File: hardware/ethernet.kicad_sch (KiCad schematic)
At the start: 41 parts, among them J1 J0011D21BNL, U22 W5500, U7 USBLC6-2P6, U9 USBLC6-2P6, Y65 25MHz

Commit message: Debugging LED added
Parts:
- R1, R12, R13, R15, R16, R17, R18, R19, R20, R21, R22, R23, R8, R80: footprint Resistor_SMD:R_0603_1608Metric -> Resistor_SMD:R_0805_2012Metric
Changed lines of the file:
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@@
 			)
 		)
-		(property "Footprint" "Resistor_SMD:R_0603_1608Metric"
+		(property "Footprint" "Resistor_SMD:R_0805_2012Metric"
 			(at 157.48 110.49 0)
 			(effects
@@
 			)
 		)
-		(property "Footprint" "Resistor_SMD:R_0603_1608Metric"
+		(property "Footprint" "Resistor_SMD:R_0805_2012Metric"
 			(at 143.51 135.89 0)
 			(effects
@@
 			)
 		)
-		(property "Footprint" "Resistor_SMD:R_0603_1608Metric"
+		(property "Footprint" "Resistor_SMD:R_0805_2012Metric"
 			(at 200.66 142.24 0)
 			(effects
@@
 			)
 		)
-		(property "Footprint" "Resistor_SMD:R_0603_1608Metric"
+		(property "Footprint" "Resistor_SMD:R_0805_2012Metric"
 			(at 128.27 92.71 0)
 			(effects
@@
 			)
 		)
-		(property "Footprint" "Resistor_SMD:R_0603_1608Metric"
+		(property "Footprint" "Resistor_SMD:R_0805_2012Metric"
 			(at 177.8 72.39 0)
 			(effects
@@
 			)
 		)
-		(property "Footprint" "Resistor_SMD:R_0603_1608Metric"
+		(property "Footprint" "Resistor_SMD:R_0805_2012Metric"
 			(at 68.58 110.49 0)
 			(effects
@@
 			)
 		)
-		(property "Footprint" "Resistor_SMD:R_0603_1608Metric"
+		(property "Footprint" "Resistor_SMD:R_0805_2012Metric"
 			(at 128.27 99.06 0)
 			(effects
@@
 			)
 		)
-		(property "Footprint" "Resistor_SMD:R_0603_1608Metric"
+		(property "Footprint" "Resistor_SMD:R_0805_2012Metric"
 			(at 160.02 72.39 0)
 			(effects
@@
 			)
 		)
-		(property "Footprint" "Resistor_SMD:R_0603_1608Metric"
+		(property "Footprint" "Resistor_SMD:R_0805_2012Metric"
 			(at 148.59 110.49 0)
 			(effects
@@
 			)
 		)
-		(property "Footprint" "Resistor_SMD:R_0603_1608Metric"
+		(property "Footprint" "Resistor_SMD:R_0805_2012Metric"
 			(at 58.42 118.11 0)
 			(effects
@@
 			)
 		)
-		(property "Footprint" "Resistor_SMD:R_0603_1608Metric"
+		(property "Footprint" "Resistor_SMD:R_0805_2012Metric"
 			(at 168.91 72.39 0)
 			(effects
@@
 			)
 		)
-		(property "Footprint" "Resistor_SMD:R_0603_1608Metric"
+		(property "Footprint" "Resistor_SMD:R_0805_2012Metric"
 			(at 128.27 80.01 0)
 			(effects
@@
 			)
 		)
-		(property "Footprint" "Resistor_SMD:R_0603_1608Metric"
+		(property "Footprint" "Resistor_SMD:R_0805_2012Metric"
 			(at 201.93 134.62 0)
 			(effects
@@
 			)
 		)
-		(property "Footprint" "Resistor_SMD:R_0603_1608Metric"
+		(property "Footprint" "Resistor_SMD:R_0805_2012Metric"
 			(at 128.27 86.36 0)
 			(effects

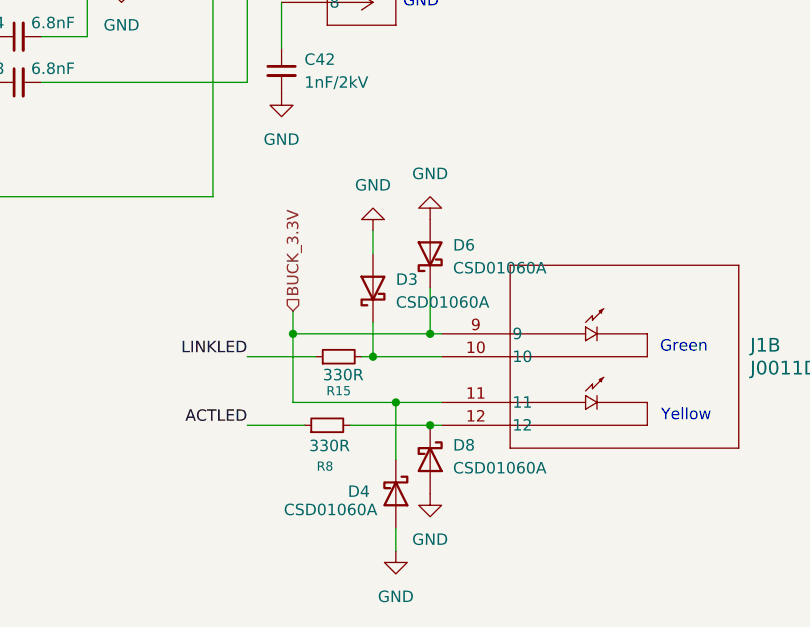
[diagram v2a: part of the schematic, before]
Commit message: removed Ethernet LED diodes
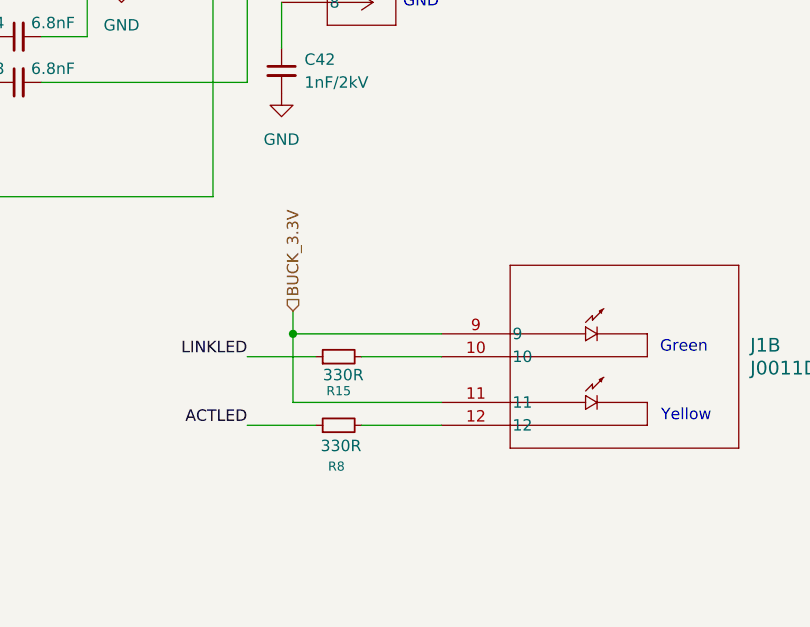
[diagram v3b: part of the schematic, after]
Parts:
- removed D3, D4, D6, D8: CSD01060A, Package_TO_SOT_THT:TO-220-2_Vertical, symbol Diode:CSD01060A
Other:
- moved on the sheet: R8

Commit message: Replaced 3.3V symbol
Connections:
- net BUCK_3.3V renamed +3.3V

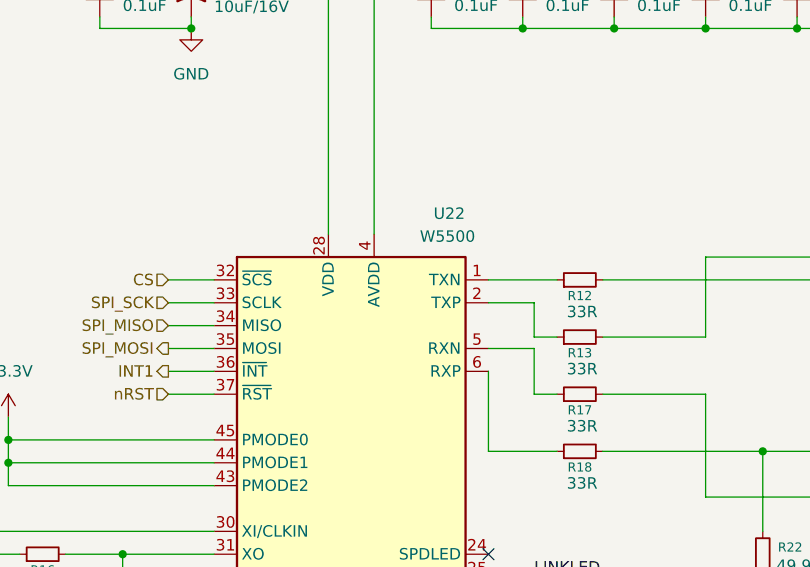
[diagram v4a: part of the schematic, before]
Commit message: updated major symbol and footprints
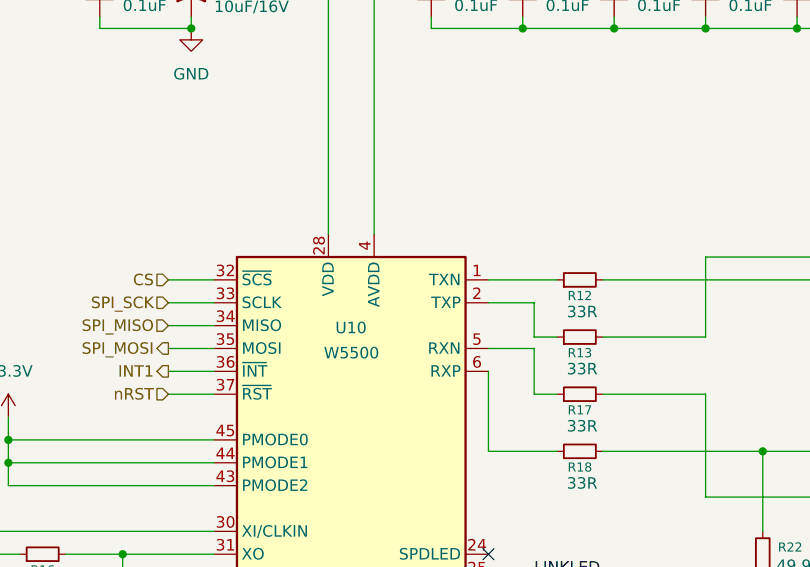
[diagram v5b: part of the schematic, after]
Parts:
- removed U22: W5500, Package_QFP:LQFP-48_7x7mm_P0.5mm, symbol Interface_Ethernet:W5500
- added U10: W5500, Package_QFP:LQFP-48_7x7mm_P0.5mm, symbol Interface_Ethernet:W5500
- J1: footprint Custom_Parts:CONN_J0011D21B_PUL -> pyronet_footprints:CONN_J0011D21B_PUL; symbol 2026-02-18_03-44-30:J0011D21BNL -> pyronet_symbols:J0011D21BNL
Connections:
- net +3.3V: now also U10.28 (VDD), U10.43 (PMODE2), U10.44 (PMODE1), U10.45 (PMODE0)
- net +3.3VA: now also U10.11 (AVDD), U10.15 (AVDD), U10.17 (AVDD), U10.21 (AVDD), U10.4 (AVDD), U10.8 (AVDD)
- net ACTLED: now also U10.27 (ACTLED)
- net CS: now also U10.32 (~{SCS})
- net GND: now also U10.14 (AGND), U10.16 (AGND), U10.19 (AGND), U10.29 (GND), U10.3 (AGND), U10.48 (AGND), U10.9 (AGND)
- net INT1: now also U10.36 (~{INT})
- net LINKLED: now also U10.25 (LINKLED)
- net SPI_MISO: now also U10.34 (MISO)
- net SPI_MOSI: now also U10.35 (MOSI)
- net SPI_SCK: now also U10.33 (SCLK)
- net nRST: now also U10.37 (~{RST})
- net at C29.1: now also U10.20 (TOCAP)
- net at R1.1: now also U10.10 (EXRES1)
- net at C28.1: now also U10.22 (1V2O)
- net at R17.1: now also U10.5 (RXN)
- net at R12.1: now also U10.1 (TXN)
- net at R13.1: now also U10.2 (TXP)
- net at R16.1, R80.1: now also U10.30 (XI/CLKIN)
- net at C8.1, R16.2, Y65.3: now also U10.31 (XO)
- net at R18.1: now also U10.6 (RXP)
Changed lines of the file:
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@@
 	)
 	(symbol
-		(lib_id "2026-02-18_03-44-30:J0011D21BNL")
+		(lib_id "pyronet_symbols:J0011D21BNL")
 		(at 213.36 132.08 0)
 		(unit 2)
@@
 			)
 		)
-		(property "Footprint" "Custom_Parts:CONN_J0011D21B_PUL"
+		(property "Footprint" "pyronet_footprints:CONN_J0011D21B_PUL"
 			(at 213.36 132.08 0)
 			(effects
@@
 	)
 	(symbol
-		(lib_id "Interface_Ethernet:W5500")
-		(at 102.87 105.41 0)
-		(unit 1)
-		(exclude_from_sim no)
-		(in_bom yes)
-		(on_board yes)
-		(dnp no)
-		(property "Reference" "U22"
-			(at 112.014 72.644 0)
-			(effects
-				(font
-					(size 1.27 1.27)
-				)
-				(justify left)
-			)
-		)
-		(property "Value" "W5500"
-			(at 110.49 75.184 0)
-			(effects
-				(font
-					(size 1.27 1.27)
-				)
-				(justify left)
-			)
-		)
-		(property "Footprint" "Package_QFP:LQFP-48_7x7mm_P0.5mm"
-			(at 102.87 63.5 0)
-			(effects
-				(font
-					(size 1.27 1.27)
-				)
-				(hide yes)
-			)
-		)
-		(property "Datasheet" "http://wizwiki.net/wiki/lib/exe/fetch.php/products:w5500:w5500_ds_v109e.pdf"
-			(at 102.87 80.01 0)
-			(effects
-				(font
-					(size 1.27 1.27)
-				)
-				(hide yes)
-			)
-		)
-		(property "Description" "10/100Mb SPI Ethernet controller with TCP/IP stack, LQFP-48"
-			(at 102.87 105.41 0)
-			(effects
-				(font
-					(size 1.27 1.27)
-				)
-				(hide yes)
-			)
-		)
-		(pin "36"
-		)
-		(pin "45"
-		)
-		(pin "30"
-		)
-		(pin "38"
-		)
-		(pin "40"
-		)
-		(pin "42"
-		)
-		(pin "34"
-		)
-		(pin "32"
-		)
-		(pin "35"
-		)
-		(pin "33"
-		)
-		(pin "37"
-		)
-		(pin "44"
-		)
-		(pin "43"
-		)
-		(pin "31"
-		)
-		(pin "39"
-		)
-		(pin "41"
-		)
-		(pin "19"
-		)
-		(pin "3"
-		)
-		(pin "1"
-		)
-		(pin "26"
-		)
-		(pin "28"
-		)
-		(pin "46"
-		)
-		(pin "20"
-		)
-		(pin "11"
-		)
-		(pin "17"
-		)
-		(pin "14"
-		)
-		(pin "16"
-		)
-		(pin "13"
-		)
-		(pin "2"
-		)
-		(pin "23"
-		)
-		(pin "29"
-		)
-		(pin "15"
-		)
-		(pin "4"
-		)
-		(pin "8"
-		)
-		(pin "12"
-		)
-		(pin "9"
-		)
-		(pin "7"
-		)
-		(pin "47"
-		)
-		(pin "21"
-		)
-		(pin "5"
-		)
-		(pin "48"
-		)
-		(pin "6"
-		)
-		(pin "24"
-		)
-		(pin "25"
-		)
-		(pin "27"
-		)
-		(pin "10"
-		)
-		(pin "18"
-		)
-		(pin "22"
-		)
-		(instances
-			(project "Senior_Design"
-				(path "/8f5928e8-0fc1-4443-a20f-3bfeb956761e/d4b85e6c-5f5c-4400-806e-353edbeb9b74"
-					(reference "U22")
-					(unit 1)
-				)
-			)
-		)
-	)
-	(symbol
 		(lib_id "Device:C_Small")
 		(at 166.37 99.06 90)
@@
 	)
 	(symbol
+		(lib_id "Interface_Ethernet:W5500")
+		(at 102.87 105.41 0)
+		(unit 1)
+		(exclude_from_sim no)
+		(in_bom yes)
+		(on_board yes)
+		(dnp no)
+		(property "Reference" "U10"
+			(at 101.092 85.344 0)
+			(effects
+				(font
+					(size 1.27 1.27)
+				)
+				(justify left)
+			)
+		)
+		(property "Value" "W5500"
+			(at 99.822 88.138 0)
+			(effects
+				(font
+					(size 1.27 1.27)
+				)
+				(justify left)
+			)
+		)
+		(property "Footprint" "Package_QFP:LQFP-48_7x7mm_P0.5mm"
+			(at 102.87 63.5 0)
+			(effects
+				(font
+					(size 1.27 1.27)
+				)
+				(hide yes)
+			)
+		)
+		(property "Datasheet" "http://wizwiki.net/wiki/lib/exe/fetch.php/products:w5500:w5500_ds_v109e.pdf"
+			(at 102.87 80.01 0)
+			(effects
+				(font
+					(size 1.27 1.27)
+				)
+				(hide yes)
+			)
+		)
+		(property "Description" "10/100Mb SPI Ethernet controller with TCP/IP stack, LQFP-48"
+			(at 102.87 105.41 0)
+			(effects
+				(font
+					(size 1.27 1.27)
+				)
+				(hide yes)
+			)
+		)
+		(pin "32"
+		)
+		(pin "21"
+		)
+		(pin "14"
+		)
+		(pin "19"
+		)
+		(pin "4"
+		)
+		(pin "16"
+		)
+		(pin "8"
+		)
+		(pin "3"
+		)
+		(pin "48"
+		)
+		(pin "17"
+		)
+		(pin "43"
+		)
+		(pin "35"
+		)
+		(pin "44"
+		)
+		(pin "45"
+		)
+		(pin "37"
+		)
+		(pin "36"
+		)
+		(pin "34"
+		)
+		(pin "30"
+		)
+		(pin "15"
+		)
+		(pin "11"
+		)
+		(pin "29"
+		)
+		(pin "28"
+		)
+		(pin "23"
+		)
+		(pin "42"
+		)
+		(pin "41"
+		)
+		(pin "40"
+		)
+		(pin "39"
+		)
+		(pin "38"
+		)
+		(pin "31"
+		)
+		(pin "33"
+		)
+		(pin "9"
+		)
+		(pin "7"
+		)
+		(pin "12"
+		)
+		(pin "13"
+		)
+		(pin "46"
+		)
+		(pin "47"
+		)
+		(pin "1"
+		)
+		(pin "2"
+		)
+		(pin "5"
+		)
+		(pin "6"
+		)
+		(pin "24"
+		)
+		(pin "25"
+		)
+		(pin "26"
+		)
+		(pin "27"
+		)
+		(pin "10"
+		)
+		(pin "18"
+		)
+		(pin "20"
+		)
+		(pin "22"
+		)
+		(instances
+			(project ""
+				(path "/8f5928e8-0fc1-4443-a20f-3bfeb956761e/d4b85e6c-5f5c-4400-806e-353edbeb9b74"
+					(reference "U10")
+					(unit 1)
+				)
+			)
+		)
+	)
+	(symbol
 		(lib_id "Device:R_Small")
 		(at 68.58 110.49 90)
@@
 	)
 	(symbol
-		(lib_name "J0011D21BNL_1")
-		(lib_id "2026-02-18_03-44-30:J0011D21BNL")
+		(lib_id "pyronet_symbols:J0011D21BNL")
 		(at 195.58 77.47 0)
 		(unit 1)
@@
 			)
 		)
-		(property "Footprint" "Custom_Parts:CONN_J0011D21B_PUL"
+		(property "Footprint" "pyronet_footprints:CONN_J0011D21B_PUL"
 			(at 195.58 77.47 0)
 			(effects

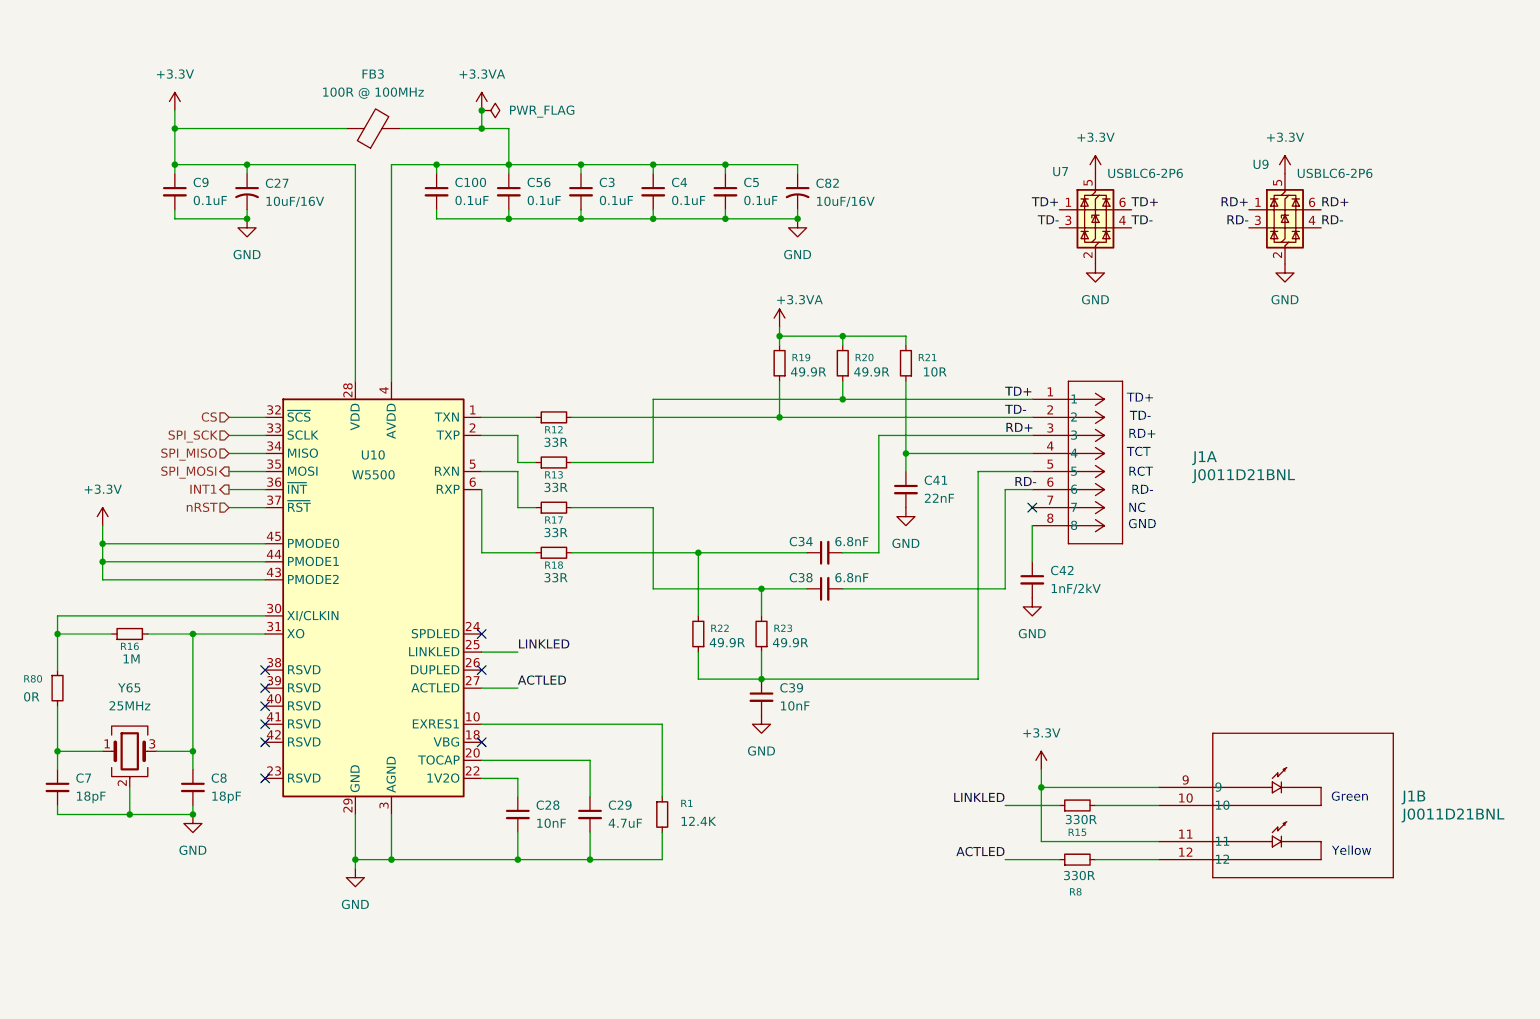
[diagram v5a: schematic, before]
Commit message: updated 5V power and pin
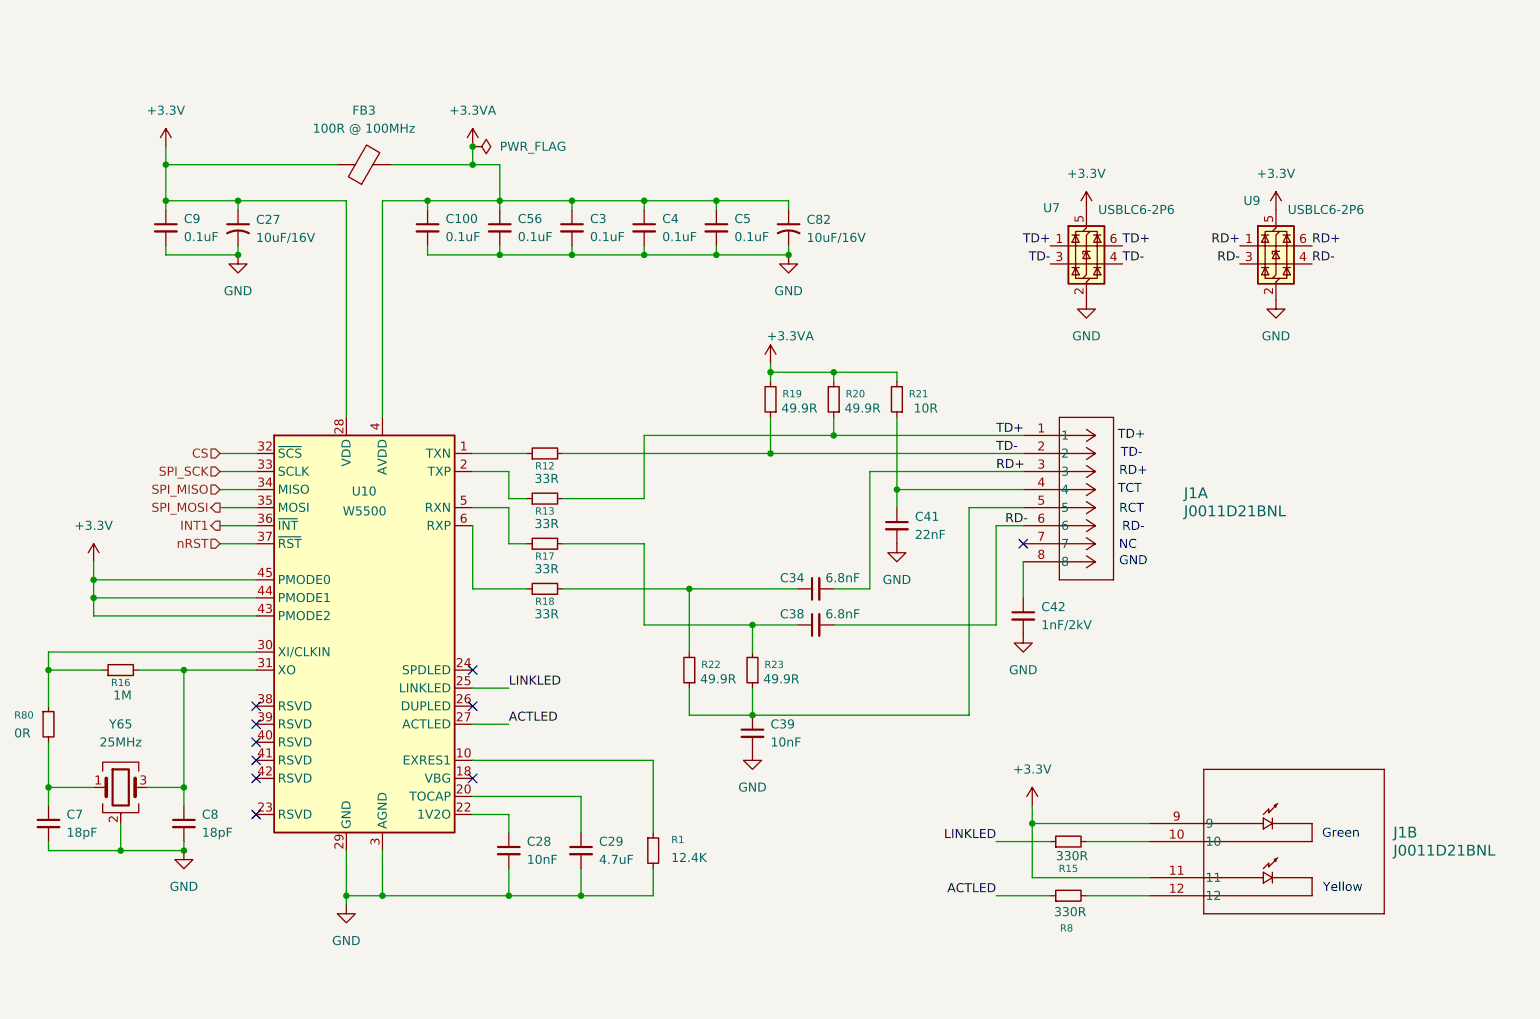
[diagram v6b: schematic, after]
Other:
- moved on the sheet: C100, C27, C28, C29, C3, C34, C38, C39, C4, C41, C42, C5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

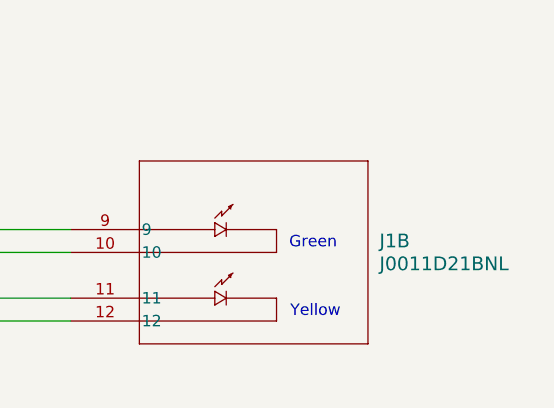
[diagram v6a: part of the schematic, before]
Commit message: passing ERC w/ exclusions
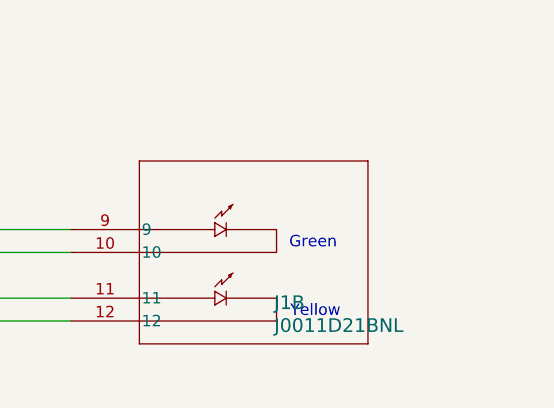
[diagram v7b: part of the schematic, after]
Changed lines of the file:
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@@
 		(fields_autoplaced yes)
 		(property "Reference" "J1"
-			(at 246.38 138.4299 0)
+			(at 234.696 145.288 0)
 			(effects
 				(font
@@
 		)
 		(property "Value" "J0011D21BNL"
-			(at 246.38 140.9699 0)
+			(at 234.696 147.828 0)
 			(effects
 				(font
@@
 	)
 	(symbol
+		(lib_name "J0011D21BNL_1")
 		(lib_id "pyronet_symbols:J0011D21BNL")
 		(at 194.31 82.55 0)

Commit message: updated annotations
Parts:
- renumbered C7 to C701, C9 to C702, C8 to C703, C27 to C704, C100 to C705, C56 to C706, C28 to C707, C3 to C708, C29 to C709, C4 to C710, C5 to C711, C39 to C712, C82 to C713, C34 to C714, C38 to C715, C41 to C716, C42 to C717, FB3 to FB701, J1 to J701, R80 to R701, R16 to R702, R12 to R703, R13 to R704, R17 to R705, R18 to R706, R1 to R707, R22 to R708, R23 to R709, R19 to R710, R20 to R711, R21 to R712, R15 to R713, R8 to R714, U10 to U701, U7 to U702, U9 to U703, Y65 to Y701
